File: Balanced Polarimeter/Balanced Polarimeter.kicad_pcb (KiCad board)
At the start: 2 copper layers, 52 x 46 mm, 15 parts, among them IC1 OP27, Q1 MMPQ3904, Q2 MMPQ3904, U1 ADA4898-1YRDZ, U2 ADA4898-1YRDZ

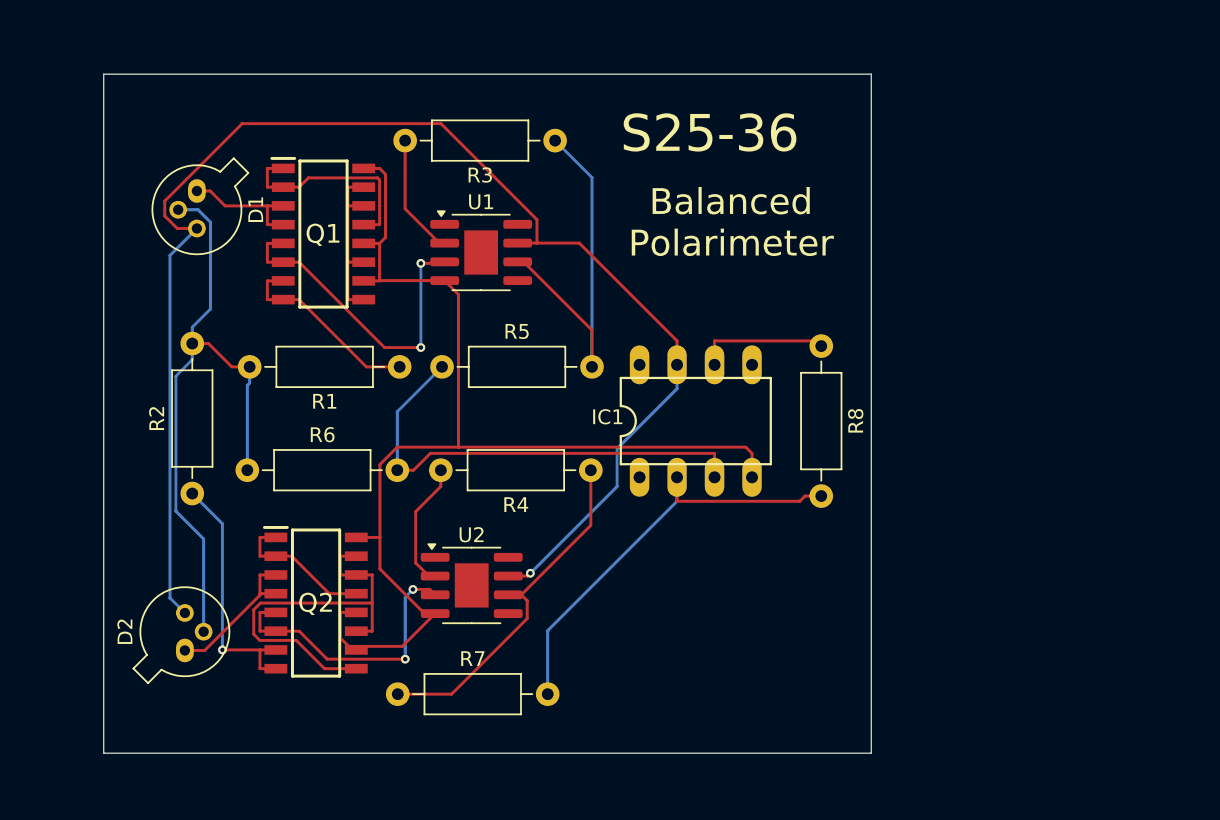
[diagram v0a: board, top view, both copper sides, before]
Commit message: Added BNC
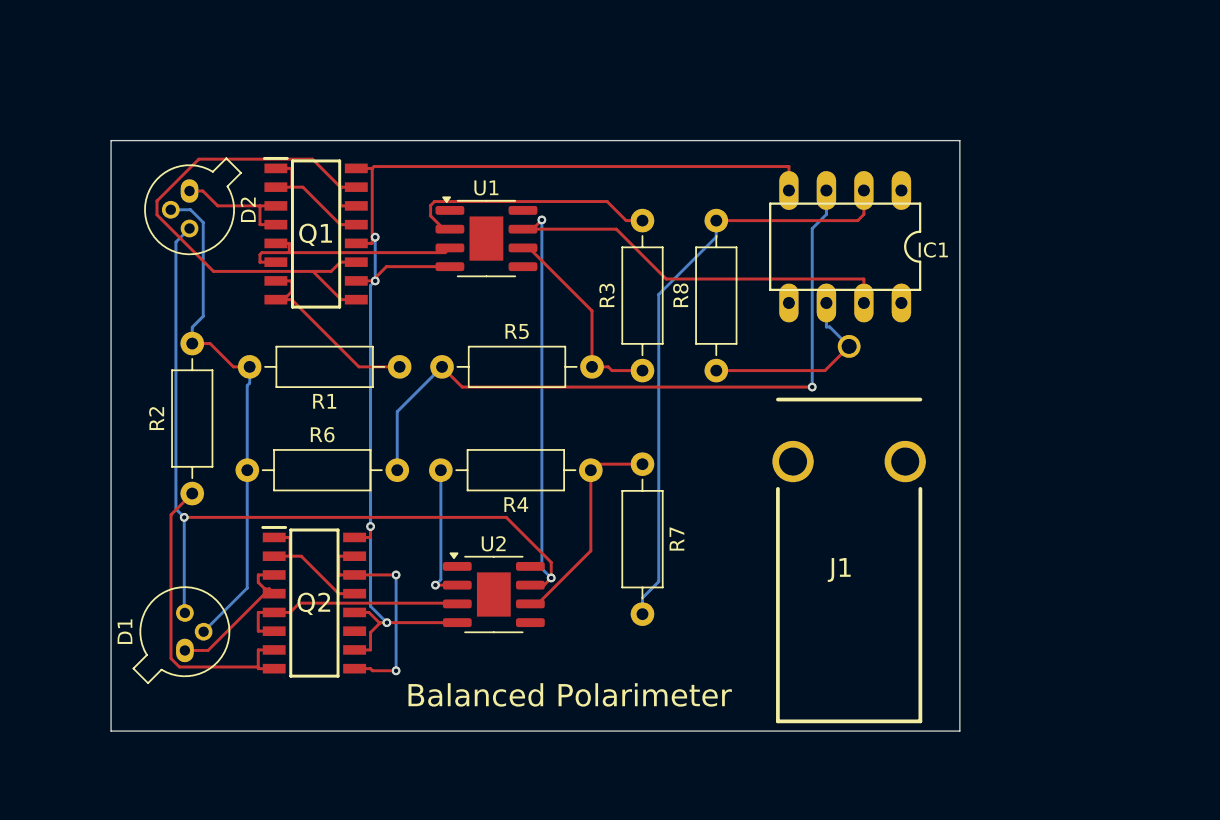
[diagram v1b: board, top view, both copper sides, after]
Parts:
- added J1: 73100-0105, Senior Design:73100-0105, F.Cu at (177.5, 103.3)
- moved R7 22.8 mm to (163.5, 85.9), turned to -90 degrees
- moved R3 16.7 mm to (163.5, 79.6), turned to 90 degrees
- moved IC1 15.6 mm to (177.2, 71.2), turned to 180 degrees
- moved R8 7.30 mm to (168.5, 79.6), turned to 90 degrees
- moved U2 1.62 mm to (153.4, 94.8)
- moved U1 1.01 mm to (152.9, 70.6)
- moved D2 0.50 mm to (132.8, 67.4)
- moved Q1 0.50 mm to (141.4, 70.3)
- moved Q2 0.11 mm to (141.3, 95.3)
- renumbered D2 to D1, D1 to D2
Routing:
- net Net-(Q1-BASE_#1): track 11.9 -> 37.9 mm
- net Net-(IC1-Pad3): track 31.8 -> 47.6 mm, vias 0 -> 1
- net Net-(R3-Pad1): track 25.8 -> 13.8 mm
- net Net-(Q2-BASE_#1): track 27.2 -> 15.6 mm, vias 0 -> 2
- net Net-(IC1-Pad2): track 29.9 -> 40.5 mm
- net +5V: track 97.4 -> 107.6 mm, vias 1 -> 3
- net Net-(R4-Pad1): track 23.9 -> 14.7 mm
- net Net-(U1--): track 8.26 -> 17.4 mm
- net GND: track 43.6 -> 34.8 mm
- net Net-(Q1-COLLECTOR_#3_1): track 22.5 -> 16.2 mm, vias 2 -> 0
- net Net-(Q1-BASE_#2): track 14.4 -> 8.85 mm
- net V_out: track 9.00 -> 13.4 mm
- net -5V: track 79.0 -> 83.2 mm, vias 0 -> 4
- net Net-(Q2-COLLECTOR_#4_1): track 17.4 -> 21.3 mm, vias 1 -> 0
- net Net-(Q2-COLLECTOR_#3_1): track 19.6 -> 16.1 mm, vias 2 -> 0
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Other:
- board size 52 x 46 mm -> 57.5 x 40 mm
- board text removed: "S25-36"

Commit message: Updates
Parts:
- added H1: MountingHole, MountingHole:MountingHole_2.1mm, F.Cu at (125.5, 60.0)
- added H2: MountingHole, MountingHole:MountingHole_2.1mm, F.Cu at (189.5, 60.0)
- added H3: MountingHole, MountingHole:MountingHole_2.1mm, F.Cu at (125.5, 104.5)
- added H4: MountingHole, MountingHole:MountingHole_2.1mm, F.Cu at (189.5, 104.5)
- added J2: Conn_01x03_Pin, Connector_PinHeader_1.00mm:PinHeader_1x03_P1.00mm_Vertical, F.Cu at (167.0, 60.5)
- added J3: Conn_01x03_Pin, Connector_PinHeader_1.00mm:PinHeader_1x03_P1.00mm_Vertical, F.Cu at (154.0, 60.5)
- added J4: Conn_01x02_Pin, Connector_PinHeader_1.00mm:PinHeader_1x02_P1.00mm_Vertical, F.Cu at (182.0, 67.5)
- moved J1 18.2 mm to (192.6, 93.2), turned to 90 degrees
- moved IC1 9.34 mm to (181.5, 79.5)
- moved D2 3.20 mm to (130.3, 69.4)
- moved D1 3.20 mm to (130.5, 96.0)
- moved R8 2.00 mm to (170.5, 79.6)
- moved Q1 1.43 mm to (141.2, 68.9)
- moved Q2 1.17 mm to (141.3, 96.5)
- moved U2 1.09 mm to (153.0, 95.8)
- moved R2 1.00 mm to (132.0, 87.9)
- moved R6 0.19 mm to (136.9, 86.3)
- moved U1 0.11 mm to (152.9, 70.8)
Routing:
- net +5V: track 107.6 -> 0.00 mm, vias 3 -> 0
- net -5V: track 83.2 -> 0.00 mm, vias 4 -> 0
- net Net-(IC1-Pad3): track 47.6 -> 0.00 mm, vias 1 -> 0
- net Net-(IC1-Pad2): track 40.5 -> 0.00 mm
- net Net-(Q1-BASE_#1): track 37.9 -> 0.00 mm
- net GND: track 34.8 -> 0.00 mm
- net Net-(Q2-COLLECTOR_#4_1): track 21.3 -> 0.00 mm
- net Net-(U1--): track 17.4 -> 0.00 mm
- net Net-(Q1-COLLECTOR_#3_1): track 16.2 -> 0.00 mm
- net Net-(Q2-COLLECTOR_#3_1): track 16.1 -> 0.00 mm
- net Net-(Q2-BASE_#1): track 15.6 -> 0.00 mm, vias 2 -> 0
- net Net-(R4-Pad1): track 14.7 -> 0.00 mm
- net Net-(R3-Pad1): track 13.8 -> 0.00 mm
- net V_out: track 13.4 -> 0.00 mm
- net Net-(Q1-COLLECTOR_#4_1): track 12.8 -> 0.00 mm
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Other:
- board size 57.5 x 40 mm -> 71 x 51.5 mm
- board text added: "+5V"
- board text added: "-5V"
- board text added: "GND"

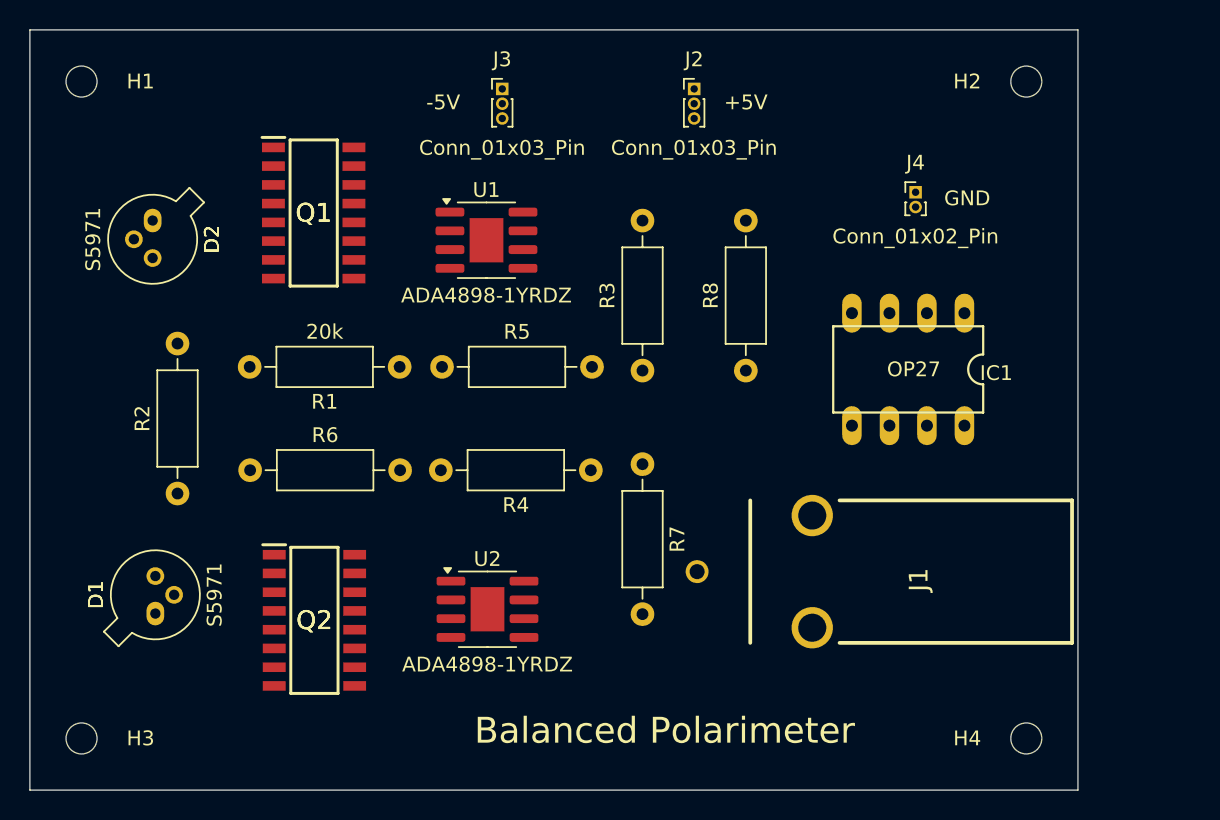
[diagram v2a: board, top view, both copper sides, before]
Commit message: Added GND Layer and 2mm Mount Holes
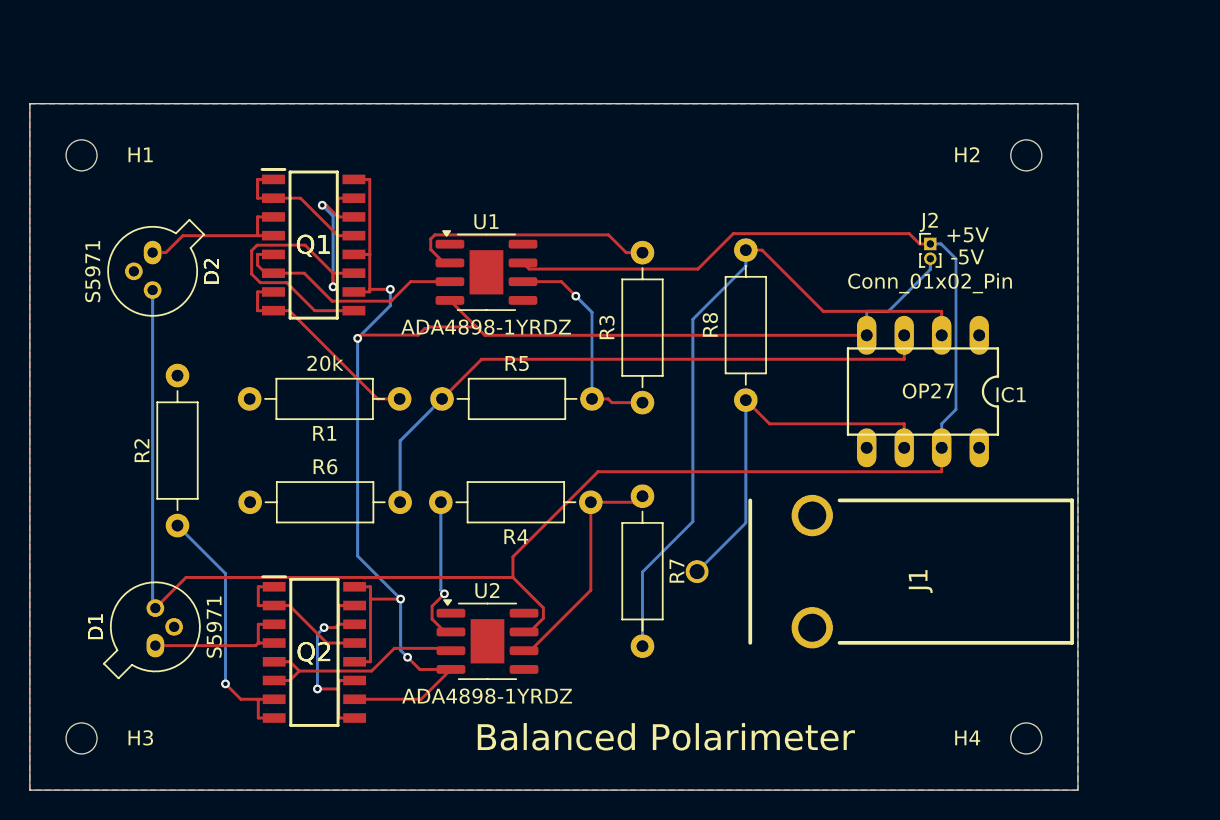
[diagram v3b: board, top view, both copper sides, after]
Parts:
- removed J3: Conn_01x03_Pin, Connector_PinHeader_1.00mm:PinHeader_1x03_P1.00mm_Vertical
- removed J4: Conn_01x02_Pin, Connector_PinHeader_1.00mm:PinHeader_1x02_P1.00mm_Vertical
- J2: value Conn_01x03_Pin -> Conn_01x02_Pin; footprint Connector_PinHeader_1.00mm:PinHeader_1x03_P1.00mm_Vertical -> Connector_PinHeader_1.00mm:PinHeader_1x02_P1.00mm_Vertical
- moved J2 19.1 mm to (183.0, 71.0)
- moved H1 5.00 mm to (125.5, 65.0)
- moved H2 5.00 mm to (189.5, 65.0)
- moved Q1 2.17 mm to (141.2, 71.1)
- moved Q2 2.17 mm to (141.3, 98.7)
- moved R1 2.17 mm to (147.0, 81.5)
- moved R2 2.17 mm to (132.0, 90.1)
- moved R3 2.17 mm to (163.5, 81.8)
- moved R4 2.17 mm to (160.0, 88.5)
- moved R5 2.17 mm to (149.9, 81.5)
- moved R6 2.17 mm to (136.9, 88.5)
- moved R7 2.17 mm to (163.5, 88.1)
- moved U1 2.17 mm to (152.9, 72.9)
- moved U2 2.17 mm to (153.0, 97.9)
- moved D1 2.17 mm to (130.5, 98.2)
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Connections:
- J2 pad 1: unconnected-(J2-Pin_1-Pad1) -> +5V
- J2 pad 2: unconnected-(J2-Pin_2-Pad2) -> -5V
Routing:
- net +5V: track 0.00 -> 130.9 mm
- net -5V: track 0.00 -> 104.8 mm, vias 0 -> 4
- net Net-(IC1-Pad2): track 0.00 -> 46.3 mm
- net Net-(IC1-Pad3): track 0.00 -> 42.2 mm
- net Net-(Q1-BASE_#1): track 0.00 -> 29.0 mm, vias 0 -> 2
- net V_out: track 0.00 -> 26.0 mm
- net Net-(Q2-COLLECTOR_#4_1): track 0.00 -> 18.1 mm, vias 0 -> 1
- net Net-(U1--): track 0.00 -> 17.4 mm
- net Net-(Q1-COLLECTOR_#3_1): track 0.00 -> 16.4 mm
- net Net-(R4-Pad1): track 0.00 -> 15.9 mm
- net Net-(Q2-BASE_#1): track 0.00 -> 14.9 mm, vias 0 -> 2
- net Net-(R3-Pad1): track 0.00 -> 14.9 mm, vias 0 -> 1
- net Net-(Q2-COLLECTOR_#3_1): track 0.00 -> 14.9 mm
- net Net-(Q1-COLLECTOR_#4_1): track 0.00 -> 14.4 mm
- net Net-(D2-K): track 0.00 -> 11.0 mm
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- added copper zone on B.Cu, net GND
- added copper zone on F.Cu, net GND
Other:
- board size 71 x 51.5 mm -> 71 x 46.5 mm
- board text removed: "GND"

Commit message: BNC Revision
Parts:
- moved J1 18.5 mm to (200.5, 76.5)
- moved J2 18.0 mm to (173.0, 86.0)
- moved IC1 17.3 mm to (173.1, 95.5)
- moved H2 5.52 mm to (184.0, 64.5)
- moved H4 5.50 mm to (184.0, 104.5)
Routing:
- net +5V: track 130.9 -> 111.9 mm, vias 0 -> 3
- net Net-(Q1-COLLECTOR_#3_1): track 16.4 -> 30.3 mm, vias 0 -> 2
- net -5V: track 104.8 -> 93.5 mm, vias 4 -> 1
- net Net-(Q2-BASE_#1): track 14.9 -> 23.8 mm
- net Net-(IC1-Pad3): track 42.2 -> 35.2 mm
- net Net-(U2--): track 10.0 -> 14.9 mm
- net Net-(Q1-BASE_#1): track 29.0 -> 24.7 mm, vias 2 -> 0
- net Net-(IC1-Pad2): track 46.3 -> 43.1 mm
- net Net-(Q2-COLLECTOR_#3_1): track 14.9 -> 16.9 mm, vias 0 -> 2
- net Net-(R4-Pad1): track 15.9 -> 17.5 mm, vias 0 -> 1
- net Net-(R3-Pad1): track 14.9 -> 13.6 mm, vias 1 -> 0
- net Net-(Q1-BASE_#2): track 9.93 -> 8.85 mm
- net Net-(Q1-COLLECTOR_#4_1): track 14.4 -> 13.6 mm
- net Net-(Q2-BASE_#2): track 9.95 -> 9.14 mm
- net V_out: track 26.0 -> 25.3 mm
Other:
- board size 71 x 46.5 mm -> 65 x 46.5 mm
